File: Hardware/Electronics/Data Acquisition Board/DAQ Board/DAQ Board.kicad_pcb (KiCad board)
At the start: 4 copper layers, 105.4 x 58.9 mm, 142 parts, among them J1 Conn_01x01_Male, J10 ~CS~_TP, J11 Conn_01x01_Male, J12 START_TP, J13 Conn_01x01_Male, J14 MID_SUPPLY_TP, J15 AVDD_TP, J16 DVDD_TP, J17 Conn_01x01_Male, J18 Conn_01x01_Male, J19 Conn_01x01_Male, J2 USB_B_Mini, J3 Conn_01x01_Male, J4 DC Barrel Jack, J5 HC-05 BT Module, J6 ICSP Header, J7 VIN_RAW_TP, J8 Conn_01x01_Male, J9 Conn_01x01_Male, Q1 DMP2100U, SW10 SW_SPDT, SW11 SW_SPDT, SW2 SW_DIP_x02, SW3 SW_SPDT, SW4 SW_SPDT, SW5 SW_SPDT, SW6 SW_SPDT, SW7 SW_SPDT, SW8 SW_SPDT, SW9 SW_SPDT, U1 ATmega328P-AU, U2 MCP1755T-5002E_SOT223-5, U3 LM3480-3.3, U4 MCP1755T-5002E_SOT223-5, U5 FT232RL, Y1 16MHz

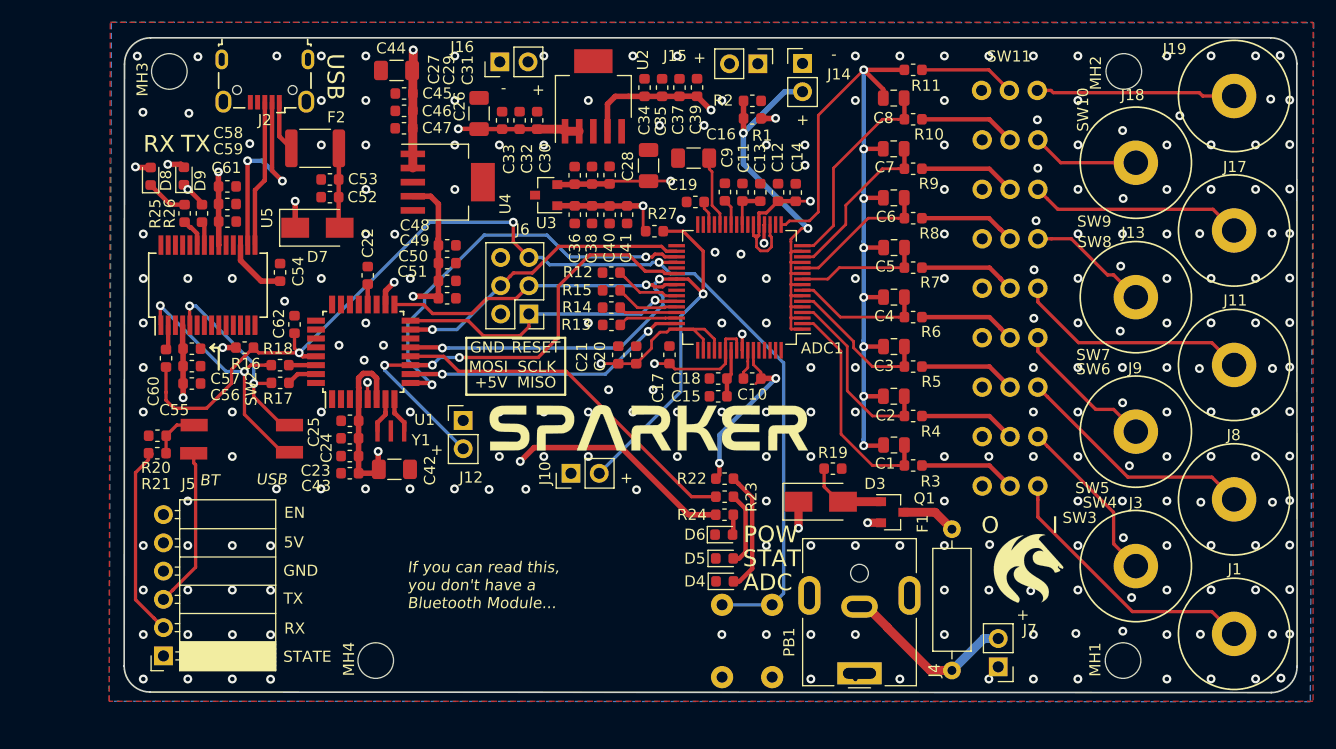
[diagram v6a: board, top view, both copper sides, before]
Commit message: Removed a stub and moved some vias. Regenerated production docs
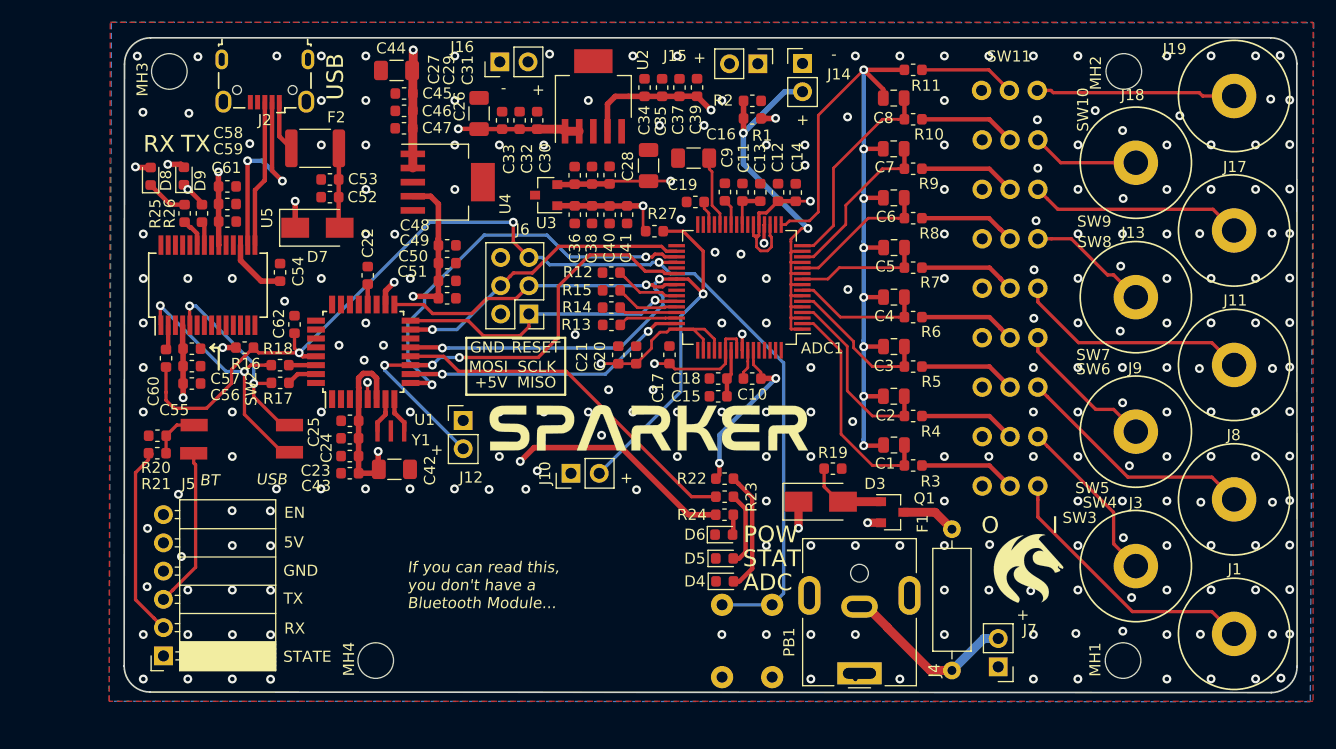
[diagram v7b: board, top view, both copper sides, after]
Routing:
- net /ADC1299/AVDD: track 65.9 -> 65.3 mm
- net /GND: vias 234 -> 235
- net (no net): vias 1 -> 0
